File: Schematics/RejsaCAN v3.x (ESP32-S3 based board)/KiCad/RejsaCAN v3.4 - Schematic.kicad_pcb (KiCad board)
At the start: 2 copper layers, 31.5 x 49.5 mm, 69 parts, among them Q1 SS8050, U1 ESP32-S3-WROOM-1(N16R8), U2 SN65HVD230DR, U3 ME2807A33M3G, U4 LMR14006XDDCR, U5 MT9700

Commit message: Enlarge U1's thermal vias to 0.3mm, clearing the last sub-tier feature
The stock ESP32-S3-WROOM-1 footprint drills its 12 thermal vias at 0.2mm, the
only feature left under JLCPCB's economical thresholds. Smallest drill on the
board is now 0.300mm, so both limits are satisfied: 5.9 mil minimum trace and
0.3mm minimum hole.

My earlier worry that this would trade one problem for another was based on a
mis-estimated pitch, read off rounded DRC coordinates. Measured properly the
vias sit on a 0.99mm pitch, so a 0.3mm drill still leaves a 0.69mm hole-to-hole
gap against JLCPCB's 0.45mm guidance -- no trade-off at all.

Only the drill changed. Growing the pad to 0.7mm as well (for a wider annular
ring) pushed a B.Cu MTDI track inside the GND clearance, so the pad stays at
0.6mm, giving a 0.15mm ring -- above this board's 0.13mm rule and far above the
0.05mm implied by JLCPCB's own via spec. One stitching via, placed when the
holes were 0.2mm, ended up 0.222mm from a thermal hole against a 0.25mm
minimum; it was one of 44 and is simply removed.

U1 moves to a project-local footprint so a library update cannot silently put
the 0.2mm drills back, matching the treatment F1 and U2 already had, and the
schematic's footprint field moves with it.

DRC: no electrical or fabrication violations. One cosmetic
lib_footprint_mismatch on U1 remains unresolved -- pad count, drills, pad sizes,
attributes, properties and 3D model all verify identical between board and
library, and fabrication output derives from the board, so it affects nothing
that gets manufactured.

Co-Authored-By: Claude Opus 5 (1M context) <noreply@anthropic.com>
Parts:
- U1: footprint RF_Module:ESP32-S3-WROOM-1 -> RejsaCAN:ESP32-S3-WROOM-1_RejsaCAN
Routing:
- net GND: vias 62 -> 61
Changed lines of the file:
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@@
 		)
 	)
-	(footprint "RF_Module:ESP32-S3-WROOM-1"
+	(footprint "RejsaCAN:ESP32-S3-WROOM-1_RejsaCAN"
 		(layer "F.Cu")
 		(at 125.848 192.9662)
@@
 			(at -2.9 1.76 90)
 			(size 0.6 0.6)
-			(drill 0.2)
+			(drill 0.3)
 			(property pad_prop_heatsink)
 			(layers "*.Cu" "F.Mask")
@@
 			(at -2.9 3.16)
 			(size 0.6 0.6)
-			(drill 0.2)
+			(drill 0.3)
 			(property pad_prop_heatsink)
 			(layers "*.Cu" "F.Mask")
@@
 			(at -2.2 1.06)
 			(size 0.6 0.6)
-			(drill 0.2)
+			(drill 0.3)
 			(property pad_prop_heatsink)
 			(layers "*.Cu" "F.Mask")
@@
 			(at -2.2 2.46)
 			(size 0.6 0.6)
-			(drill 0.2)
+			(drill 0.3)
 			(property pad_prop_heatsink)
 			(layers "*.Cu" "F.Mask")
@@
 			(at -2.2 3.86)
 			(size 0.6 0.6)
-			(drill 0.2)
+			(drill 0.3)
 			(property pad_prop_heatsink)
 			(layers "*.Cu" "F.Mask")
@@
 			(at -1.5 1.76)
 			(size 0.6 0.6)
-			(drill 0.2)
+			(drill 0.3)
 			(property pad_prop_heatsink)
 			(layers "*.Cu" "F.Mask")
@@
 			(at -1.5 3.16)
 			(size 0.6 0.6)
-			(drill 0.2)
+			(drill 0.3)
 			(property pad_prop_heatsink)
 			(layers "*.Cu" "F.Mask")
@@
 			(at -0.8 1.06)
 			(size 0.6 0.6)
-			(drill 0.2)
+			(drill 0.3)
 			(property pad_prop_heatsink)
 			(layers "*.Cu" "F.Mask")
@@
 			(at -0.8 2.46)
 			(size 0.6 0.6)
-			(drill 0.2)
+			(drill 0.3)
 			(property pad_prop_heatsink)
 			(layers "*.Cu" "F.Mask")
@@
 			(at -0.8 3.86)
 			(size 0.6 0.6)
-			(drill 0.2)
+			(drill 0.3)
 			(property pad_prop_heatsink)
 			(layers "*.Cu" "F.Mask")
@@
 			(at -0.1 1.76)
 			(size 0.6 0.6)
-			(drill 0.2)
+			(drill 0.3)
 			(property pad_prop_heatsink)
 			(layers "*.Cu" "F.Mask")
@@
 			(at -0.1 3.16)
 			(size 0.6 0.6)
-			(drill 0.2)
+			(drill 0.3)
 			(property pad_prop_heatsink)
 			(layers "*.Cu" "F.Mask")
@@
 		(size 0.7)
 		(drill 0.35)
-		(layers "F.Cu" "B.Cu")
-		(net "GND")
-	)
-	(via
-		(at 123.5 193.5)
-		(size 0.7)
-		(drill 0.35)

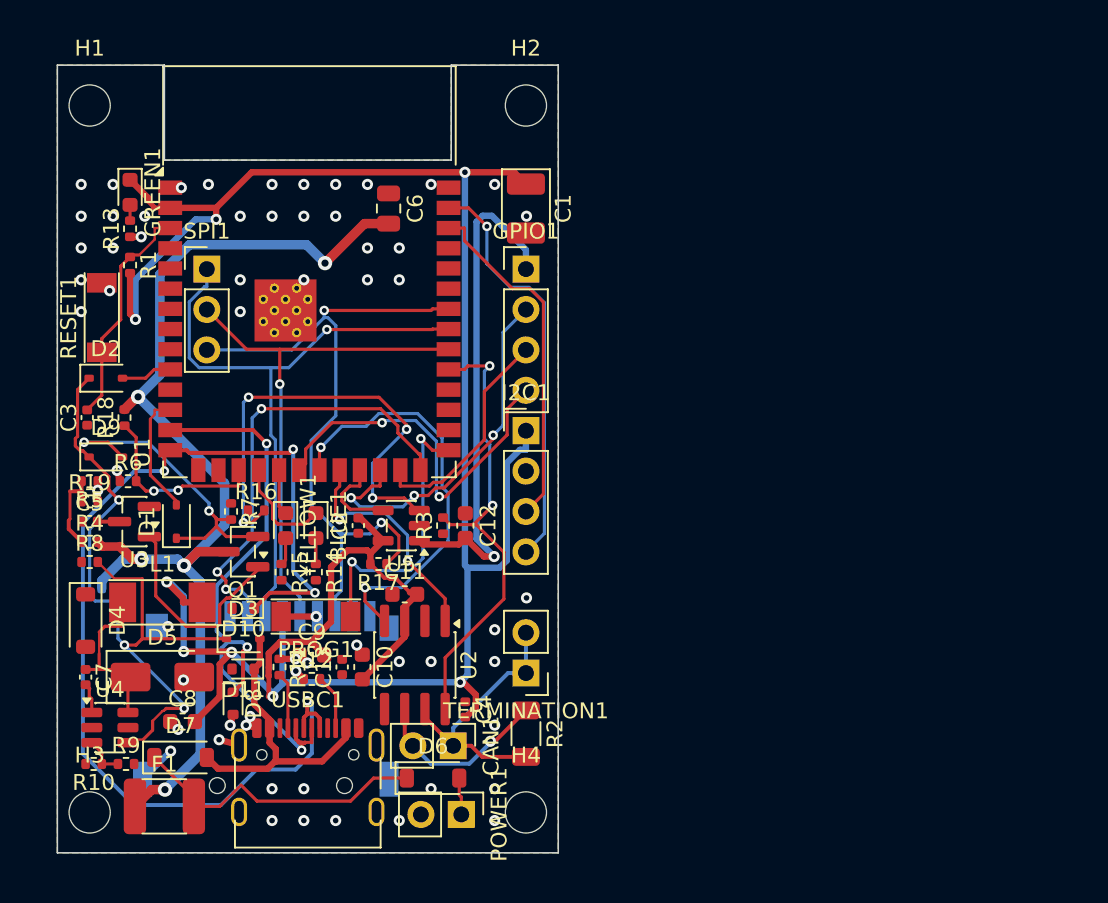
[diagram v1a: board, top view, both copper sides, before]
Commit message: PCB: 4 layers, 58mm-wide outline, all new parts placed and netted
Board rebuilt to carry the GNSS block. NOT ROUTED and placement is not
final -- see the caveats below before doing anything with this.

Done:
  - outline widened 31.5 -> 58.1 mm; H2/H4 moved out to the new right
    edge. Height and the top notch are unchanged, so USB-C and the
    other bottom-edge parts keep their edge.
  - 2 -> 4 copper layers, In1 named GND_plane, In2 PWR_plane. This is
    what the RF needs: a 50R microstrip over the bottom plane on the
    old 1.6mm 2-layer stackup would have been ~2.9mm wide, versus
    ~0.35mm over a 0.2mm prepreg to an inner plane.
  - 670 tracks, 116 vias and both pours deleted (full re-route chosen).
  - POWER1, CAN1, TERMINATION1 footprints removed; 18 new footprints
    added; 121 pad-to-net assignments synced from the schematic.
  - RF chain placed off U7's RF_IN pad: the 50R run to J2 is 3.98 mm,
    with J2 4.03 mm from the board edge.

There is no headless "update PCB from schematic" -- neither kicad-cli
nor the Python API exposes one -- so the netlist was pushed into the
board pad by pad. Any Remove()/Delete() also leaves pcbnew's SWIG
proxies returning bare SwigPyObjects for the rest of the process, even
across LoadBoard(), so stripping and building had to run as two
separate processes with every proxy bound before the first removal.

DRC: 266 violations, 244 unconnected (unrouted, so both expected).
Of the errors, 30 are courtyard overlaps. Most are the RF front end
sitting inside U7's keepout, which is what Quectel asks for -- "place
L1, C4 and C5 close to the antenna interface". One is not benign:

  U1 <-> U7 overlap 4.04 x 18.51 mm

That is the ESP32-S3-WROOM-1 antenna keepout, and the board is not wide
enough to clear it while still leaving room for the u.FL. WiFi at
2.4GHz beside an RTK receiver at 1.5GHz is a real coexistence question
and this needs a human decision: widen further, move the GNSS to the
opposite corner, or accept and shield.
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
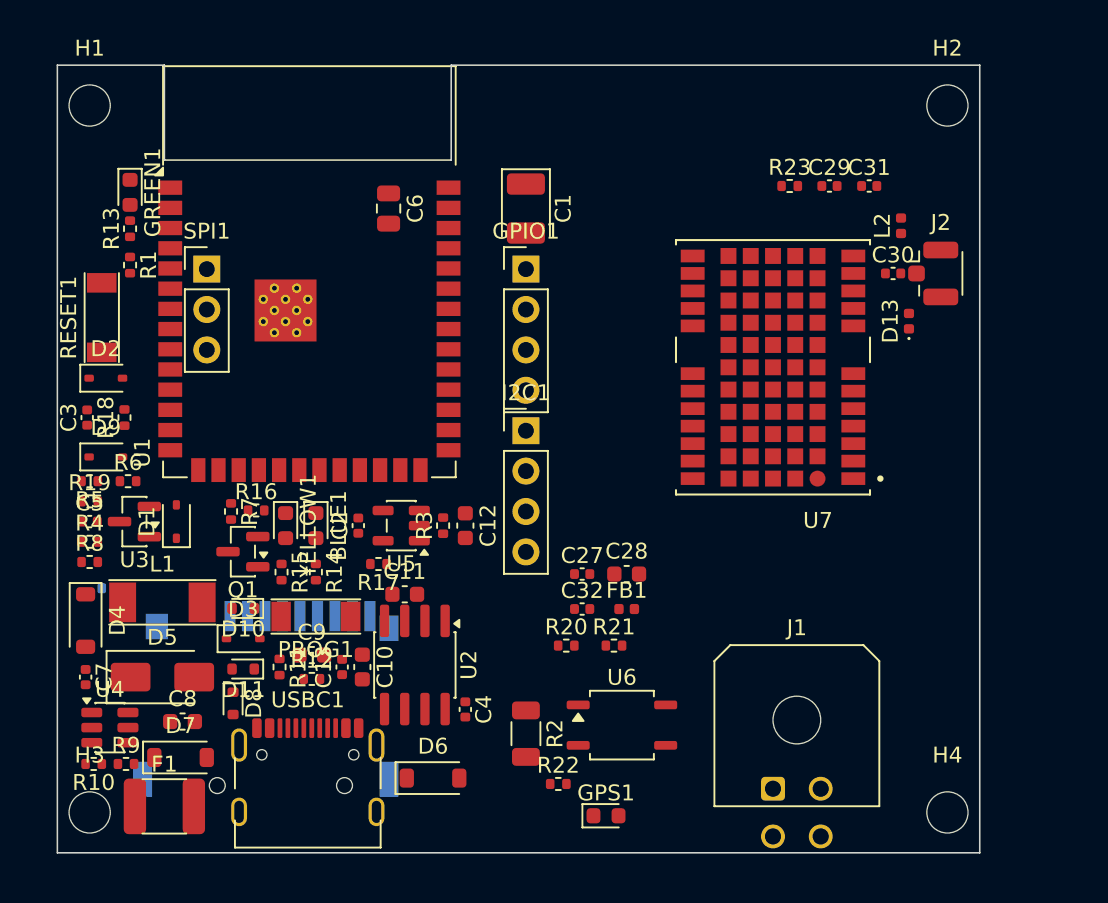
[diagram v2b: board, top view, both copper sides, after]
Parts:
- removed CAN1, POWER1, TERMINATION1: HDR-M-2.54_1x2, Connector_PinHeader_2.54mm:PinHeader_1x02_P2.54mm_Vertical
- added C27: 100nF, C_0402_1005Metric, F.Cu at (143.0, 212.0)
- added C28: 22uF, C_0603_1608Metric, F.Cu at (145.8, 212.0)
- added C29: 100nF, C_0402_1005Metric, F.Cu at (158.6, 187.6)
- added C30: 100pF, C_0402_1005Metric, F.Cu at (162.6, 193.1)
- added C31: 100pF, C_0402_1005Metric, F.Cu at (161.1, 187.6)
- added C32: 33pF, C_0402_1005Metric, F.Cu at (143.0, 214.2)
- added D13: TVS_Cj0.6pF, D_0402_1005Metric, F.Cu at (163.6, 196.1)
- added FB1: FerriteBead_600R@100MHz, L_0402_1005Metric, F.Cu at (145.8, 214.2)
- added GPS1: Blue LED, LED_0603_1608Metric, F.Cu at (144.5, 227.2)
- added J1: Micro-Fit 3.0 4P R/A, Molex_Micro-Fit_3.0_43045-0400_2x02_P3.00mm_Horizontal, F.Cu at (155.0, 225.5)
- added J2: U.FL, U.FL_Hirose_U.FL-R-SMT-1_Vertical, F.Cu at (165.6, 193.1)
- added L2: 68nH, L_0402_1005Metric, F.Cu at (163.1, 190.1)
- added R20: 500, R_0402_1005Metric, F.Cu at (142.0, 216.5)
- added R21: 10K, R_0402_1005Metric, F.Cu at (145.0, 216.5)
- added R22: 1K, R_0402_1005Metric, F.Cu at (141.5, 225.2)
- added R23: 10R, R_0402_1005Metric, F.Cu at (156.1, 187.6)
- added U6: CPC1018N, SOP-4_3.8x4.1mm_P2.54mm, F.Cu at (145.5, 221.5)
- added U7: LG290P03AAMD, LG290P03AAMD, F.Cu at (155.0, 199.0)
- moved H2 26.5 mm to (166.0, 182.5)
- moved H4 26.5 mm to (166.0, 227.0)
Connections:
- R2 pad 2: CAN_H -> TERM_SW
- U1 pad 8: GPIO15 -> GPS_LOCK
- U1 pad 9: GPIO16 -> TERM_EN
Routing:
- net 3V3: track 152.9 -> 0.00 mm, vias 8 -> 0
- net VCC: track 70.5 -> 0.00 mm, vias 5 -> 0
- net USB_D+: track 68.0 -> 0.00 mm, vias 4 -> 0
- net Net-(D2-K): track 45.6 -> 0.00 mm, vias 3 -> 0
- net MTDI: track 43.7 -> 0.00 mm, vias 2 -> 0
- net MTDO: track 39.7 -> 0.00 mm, vias 1 -> 0
- net USB_D-: track 37.3 -> 0.00 mm, vias 3 -> 0
- net MTCK: track 33.5 -> 0.00 mm, vias 1 -> 0
- net 3V3_SWITCHED: track 32.3 -> 0.00 mm, vias 1 -> 0
- net CAN_RS: track 29.7 -> 0.00 mm, vias 2 -> 0
- net Net-(U5-SET): track 29.1 -> 0.00 mm, vias 4 -> 0
- net SD_CARD: track 27.9 -> 0.00 mm, vias 3 -> 0
- net CAN_RX: track 26.3 -> 0.00 mm, vias 2 -> 0
- net SDA: track 26.0 -> 0.00 mm, vias 1 -> 0
- net GPIO12: track 23.7 -> 0.00 mm, vias 2 -> 0
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- removed copper zone on B.Cu, net GND
- removed copper zone on F.Cu, net GND
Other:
- board size 31.5 x 49.5 mm -> 58 x 49.5 mm
- copper layers 2 -> 4

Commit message: Dedicated LDO for the GNSS, and an L-shaped bump-out instead of a wide board
Two changes asked for: give the GNSS its own regulator, and stop
widening the whole board just to fit the module.

LDO
---
FB1's ferrite pi filter is gone; U8 (AP2112K-3.3, SOT-23-5, 600 mA)
now feeds GNSS_VCC from 3V3, EN tied high, with C33 1uF on the input.
This satisfies Quectel's "do not use a switching DC-DC converter",
which the ferrite only softened.

It does not work as a straight drop-in, though, and that is the part
worth recording: the buck was set to 3.29 V and the module wants 3.3 V,
so any 3.3 V LDO fed from it would sit in dropout, where PSRR collapses
and the LDO filters nothing at all. So R9 goes 33k -> 34.8k, raising
3V3 to 0.765 x (1 + 34.8/10) = 3.427 V. That leaves 127 mV of headroom
against ~56 mV of AP2112K dropout at the module's 135 mA peak.

3.427 V is inside the recommended range of everything else on the rail
(ESP32-S3 and SN65HVD230 both 3.0-3.6 V, microSD 2.7-3.6 V, MT9700 to
5.5 V), and it lifts the GAQY212GS drive through R20 390R to 5.6 mA,
still inside its 5-30 mA window.

Outline
-------
The driver is that U1's WROOM antenna keep-out reaches x=149.9, which
is 8.4 mm past the original board edge, so the GNSS has to sit out
there no matter what. Only the module needs to, though.

The board is now L-shaped: main body 110..148, plus a bump-out
148..173 x 194..229.53 carrying U7, the RF chain, J2, the LDO and J1.
2770 mm2 of copper against 3120 mm2 if the full height had been
widened to the same reach.

The bump is on the *bottom* right deliberately. The WROOM's PCB antenna
is at the top edge, so dropping the GNSS low takes the separation from
~35 mm to ~47 mm for free.

RF_IN to J2 is 3.89 mm of 50R run, with J2 5.53 mm from the edge.

DRC
---
All electrical errors are clear: no shorts, no clearance violations, no
board-edge violations. Three were found and fixed in the process --
C30 pad 1 shorting U7 pad 12, C28 pad 1 at 0.015 mm from C33, and J1's
CAN pads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
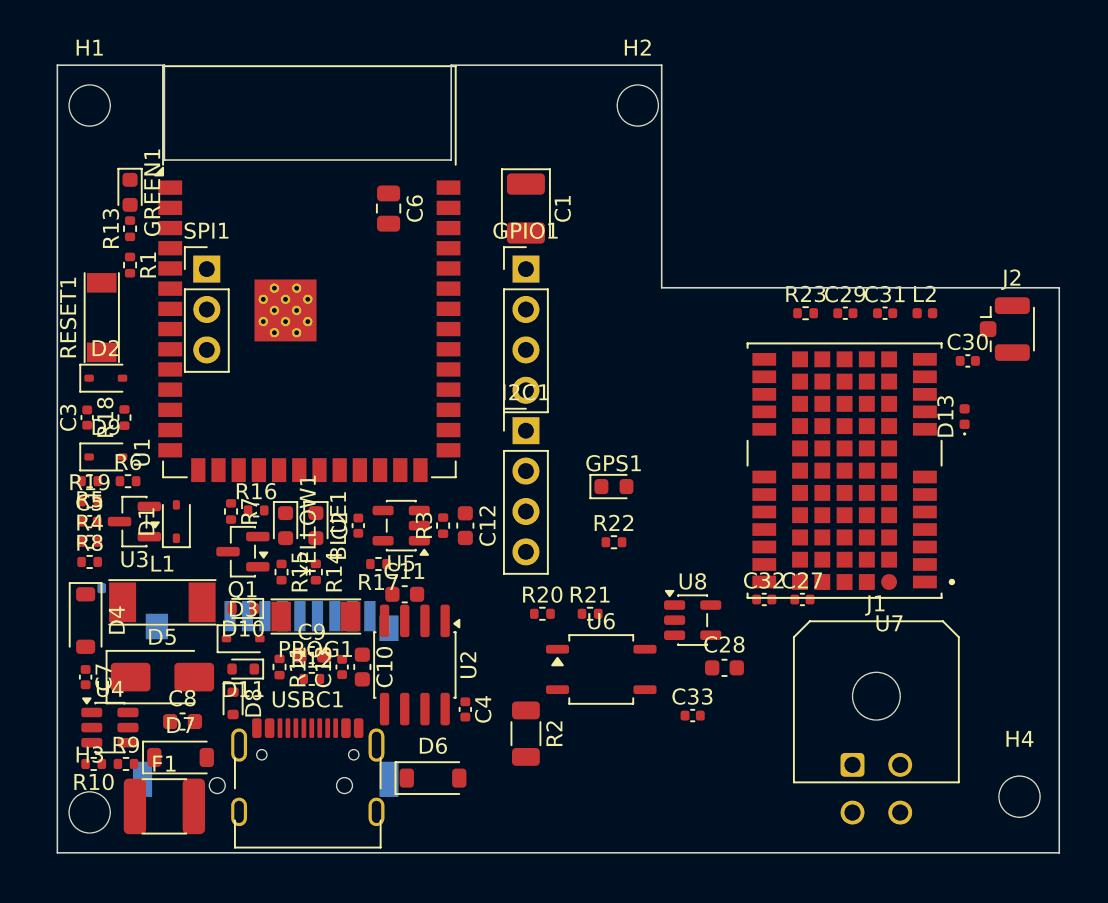
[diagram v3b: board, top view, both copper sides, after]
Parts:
- removed FB1: FerriteBead_600R@100MHz, L_0402_1005Metric
- added C33: 1uF, C_0402_1005Metric, F.Cu at (149.9, 220.9)
- added U8: AP2112K-3.3, SOT-23-5, F.Cu at (149.9, 214.9)
- moved GPS1 20.7 mm to (145.0, 206.5)
- moved H2 19.5 mm to (146.5, 182.5)
- moved R22 15.6 mm to (145.0, 210.0)
- moved C27 13.9 mm to (156.8, 213.6)
- moved C32 11.5 mm to (154.4, 213.6)
- moved C28 8.52 mm to (151.9, 217.9)
- moved C29 8.06 mm to (159.6, 195.6)
- moved C31 8.06 mm to (162.1, 195.6)
- moved R23 8.06 mm to (157.1, 195.6)
- moved U7 7.91 mm to (159.5, 205.5)
- moved C30 7.23 mm to (167.2, 198.6)
- moved D13 6.95 mm to (167.1, 202.1)
- moved J2 5.70 mm to (170.1, 196.6)
- moved L2 5.70 mm to (164.6, 195.6), turned to 0 degrees
- moved J1 5.22 mm to (160.0, 224.0)
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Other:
- board size 58 x 49.5 mm -> 63 x 49.5 mm

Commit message: Add J3, the LTE breakout: raw 12V, GND, USB_D- and USB_D+
The LTE module talks to the ESP32 over USB rather than UART, so J3
parallels the native USB pair and splits the input 12V off to feed the
module.

  J3.1  VBAT_IN   raw 12V, tapped at J1.1 ahead of D6 and F1
  J3.2  GND
  J3.3  USB_D-    GPIO19
  J3.4  USB_D+    GPIO20

The raw input net was unnamed (Net-(D6-A)); it is now VBAT_IN, carrying
J1.1, J3.1 and D6's anode.

J3 is a JST-XH 4-pin, deliberately NOT another Micro-Fit. Two identical
4-circuit Micro-Fits on one board invite plugging the CAN harness into
the USB port, which would put 12V and CAN_H directly onto USB_D+/- and
GPIO19/20. A different connector family makes that mechanically
impossible. It is also less than half the footprint area (13.49 x 6.84
vs 11.25 x 13.76), which is what let it fit at all.

Both USB lines already carry ESD diodes on the net (D8, D10), so the
new connector inherits that protection with nothing added.

Only one USB port may be connected at a time -- the ESP32-S3 is a USB
device on USBC1 and a USB host to the LTE module, and those cannot
coexist on one D+/D- pair. This is understood and accepted: the module
gets unplugged to program the board. At full speed (12 Mbps, all the
ESP32-S3 OTG supports) the unused branch is a short enough stub not to
matter.

12V for the module is tapped ahead of D6 and F1 on purpose, so the
slave does not consume this board's 1.1A fuse budget and does not push
current through a 3A Schottky. THE SLAVE MUST PROVIDE ITS OWN FUSE AND
REVERSE-POLARITY PROTECTION -- it is fed unprotected battery voltage.

Board: the bump-out grew from y=194 to y=186 to hold J3. With that the
L-shape saves 2970 vs 3120 mm2, only ~5% against a full rectangle --
the cut corner is now mostly what is left of the saving.

DRC: zero electrical and zero outline errors. What remains is 35
courtyard overlaps, 12 holes-inside-courtyard and 4 items-not-allowed,
all pre-existing classes or the GNSS decoupling that Quectel requires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
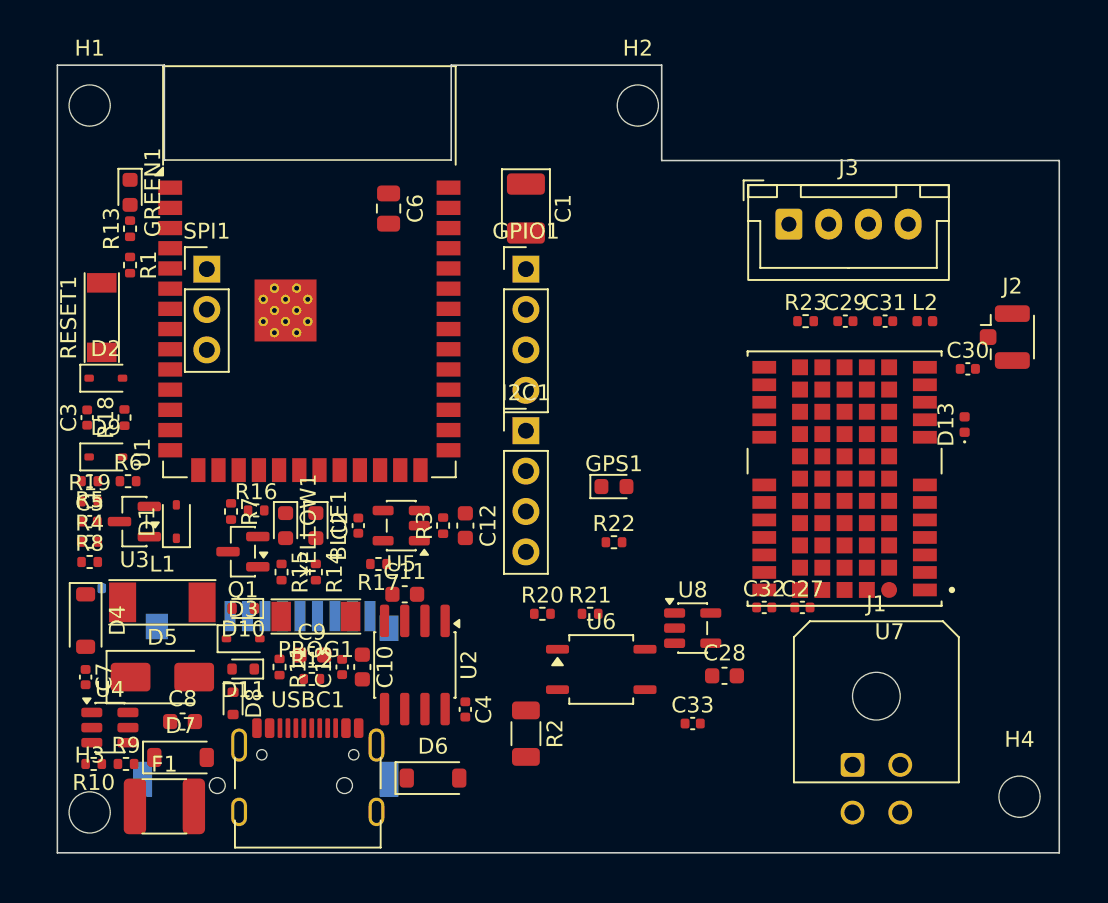
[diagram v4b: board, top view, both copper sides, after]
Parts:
- added J3: JST-XH 4P LTE, JST_XH_B4B-XH-A_1x04_P2.50mm_Vertical, F.Cu at (156.0, 190.0)
- moved C27 0.50 mm to (156.8, 214.1)
- moved C28 0.50 mm to (151.9, 218.4)
- moved C29 0.50 mm to (159.6, 196.1)
- moved C30 0.50 mm to (167.2, 199.1)
- moved C31 0.50 mm to (162.1, 196.1)
- moved C32 0.50 mm to (154.4, 214.1)
- moved C33 0.50 mm to (149.9, 221.4)
- moved D13 0.50 mm to (167.1, 202.6)
- moved J2 0.50 mm to (170.1, 197.1)
- moved L2 0.50 mm to (164.6, 196.1)
- moved R23 0.50 mm to (157.1, 196.1)
- moved U7 0.50 mm to (159.5, 206.0)
- moved U8 0.50 mm to (149.9, 215.4)
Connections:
- net Net-(D6-A) renamed VBAT_IN
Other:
- outline, holes or cut-outs redrawn
